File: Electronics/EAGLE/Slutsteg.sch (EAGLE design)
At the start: 149 parts, among them CN1 OSTYK33102030-2, CN2 OSTYK33102030-2, IC1 MC78M12CDTG, IC2 ZLDO1117G33TA, IC3 ESP32-WROVER-IE-4MB, IC4 TM8211, IC5 LM358LVIDR, IC6 TPA3244DDWR, IC7 TPA3251D2DDVR, IC8 LM324D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

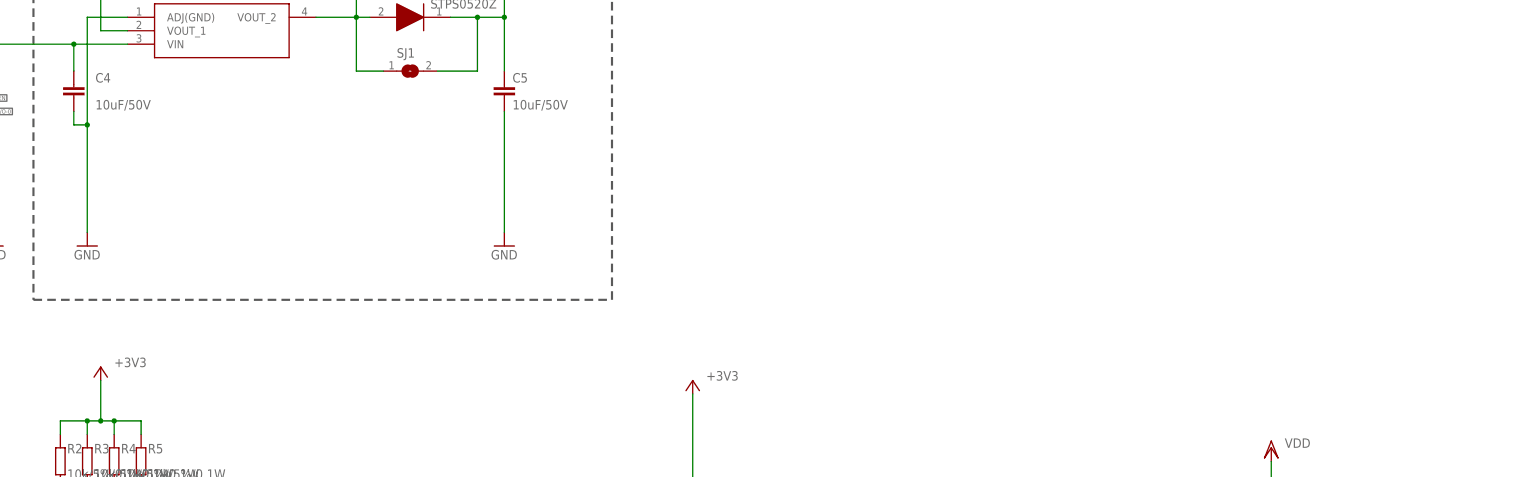
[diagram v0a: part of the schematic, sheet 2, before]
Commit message: Updated components value
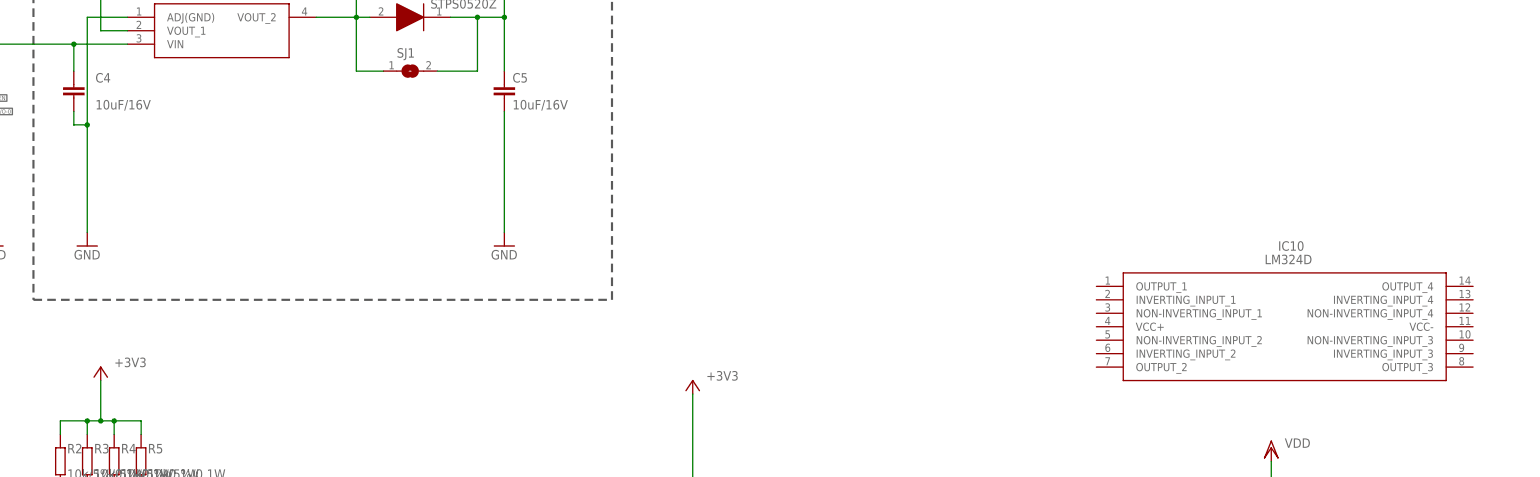
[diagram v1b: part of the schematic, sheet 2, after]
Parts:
- added CN3, CN4: OSTYK33102030-2, OSTYK33108030:OSTYK33102030-2
- added IC10: LM324D, SamacSys_Parts:LM324D
- C4, C5: value 10uF/50V -> 10uF/16V
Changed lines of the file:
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@@
 <part name="P+3" library="supply1" library_urn="urn:adsk.eagle:library:371" deviceset="+5V" device=""/>
 <part name="IC2" library="SamacSys_Parts" deviceset="ZLDO1117G33TA" device="" override_package3d_urn="urn:adsk.eagle:package:27158194/2" override_package_urn="urn:adsk.eagle:footprint:27158195/1"/>
-<part name="C5" library="rcl" library_urn="urn:adsk.eagle:library:334" deviceset="C-EU" device="C0805" package3d_urn="urn:adsk.eagle:package:23617/2" value="10uF/50V"/>
-<part name="C4" library="rcl" library_urn="urn:adsk.eagle:library:334" deviceset="C-EU" device="C0805" package3d_urn="urn:adsk.eagle:package:23617/2" value="10uF/50V"/>
+<part name="C5" library="rcl" library_urn="urn:adsk.eagle:library:334" deviceset="C-EU" device="C0805" package3d_urn="urn:adsk.eagle:package:23617/2" value="10uF/16V"/>
+<part name="C4" library="rcl" library_urn="urn:adsk.eagle:library:334" deviceset="C-EU" device="C0805" package3d_urn="urn:adsk.eagle:package:23617/2" value="10uF/16V"/>
 <part name="GND47" library="supply1" library_urn="urn:adsk.eagle:library:371" deviceset="GND" device=""/>
 <part name="D1" library="SamacSys_Parts" deviceset="STPS0520Z" device="" override_package3d_urn="urn:adsk.eagle:package:27158217/2" override_package_urn="urn:adsk.eagle:footprint:27158218/1"/>
@@
 <part name="R5" library="rcl" library_urn="urn:adsk.eagle:library:334" deviceset="R-EU_" device="R0603" package3d_urn="urn:adsk.eagle:package:23555/3" value="10k/5%/0.1W"/>
 <part name="+3V14" library="supply1" library_urn="urn:adsk.eagle:library:371" deviceset="+3V3" device=""/>
+<part name="IC10" library="SamacSys_Parts" deviceset="LM324D" device=""/>
+<part name="CN3" library="OSTYK33108030" deviceset="OSTYK33102030-2" device="" override_package3d_urn="urn:adsk.eagle:package:27162182/2" override_package_urn="urn:adsk.eagle:footprint:27162183/1"/>
+<part name="CN4" library="OSTYK33108030" deviceset="OSTYK33102030-2" device="" override_package3d_urn="urn:adsk.eagle:package:27162207/2" override_package_urn="urn:adsk.eagle:footprint:27162209/1"/>
 </parts>
 <sheets>
@@
 <instance part="CN2" gate="G$1" x="342.9" y="182.88" smashed="yes">
 <attribute name="NAME" x="342.9" y="200.66" size="1.778" layer="95"/>
+</instance>
+<instance part="CN3" gate="G$1" x="342.9" y="149.86" smashed="yes">
+<attribute name="NAME" x="342.9" y="167.64" size="1.778" layer="95"/>
+</instance>
+<instance part="CN4" gate="G$1" x="342.9" y="121.92" smashed="yes">
+<attribute name="NAME" x="342.9" y="139.7" size="1.778" layer="95"/>
 </instance>
 </instances>
@@
 <attribute name="VALUE" x="68.58" y="127" size="1.778" layer="96"/>
 </instance>
+<instance part="IC10" gate="G$1" x="254" y="142.24" smashed="yes">
+<attribute name="NAME" x="288.29" y="149.86" size="1.778" layer="95" align="center-left"/>
+<attribute name="VALUE" x="285.75" y="147.32" size="1.778" layer="96" align="center-left"/>
+</instance>
 </instances>

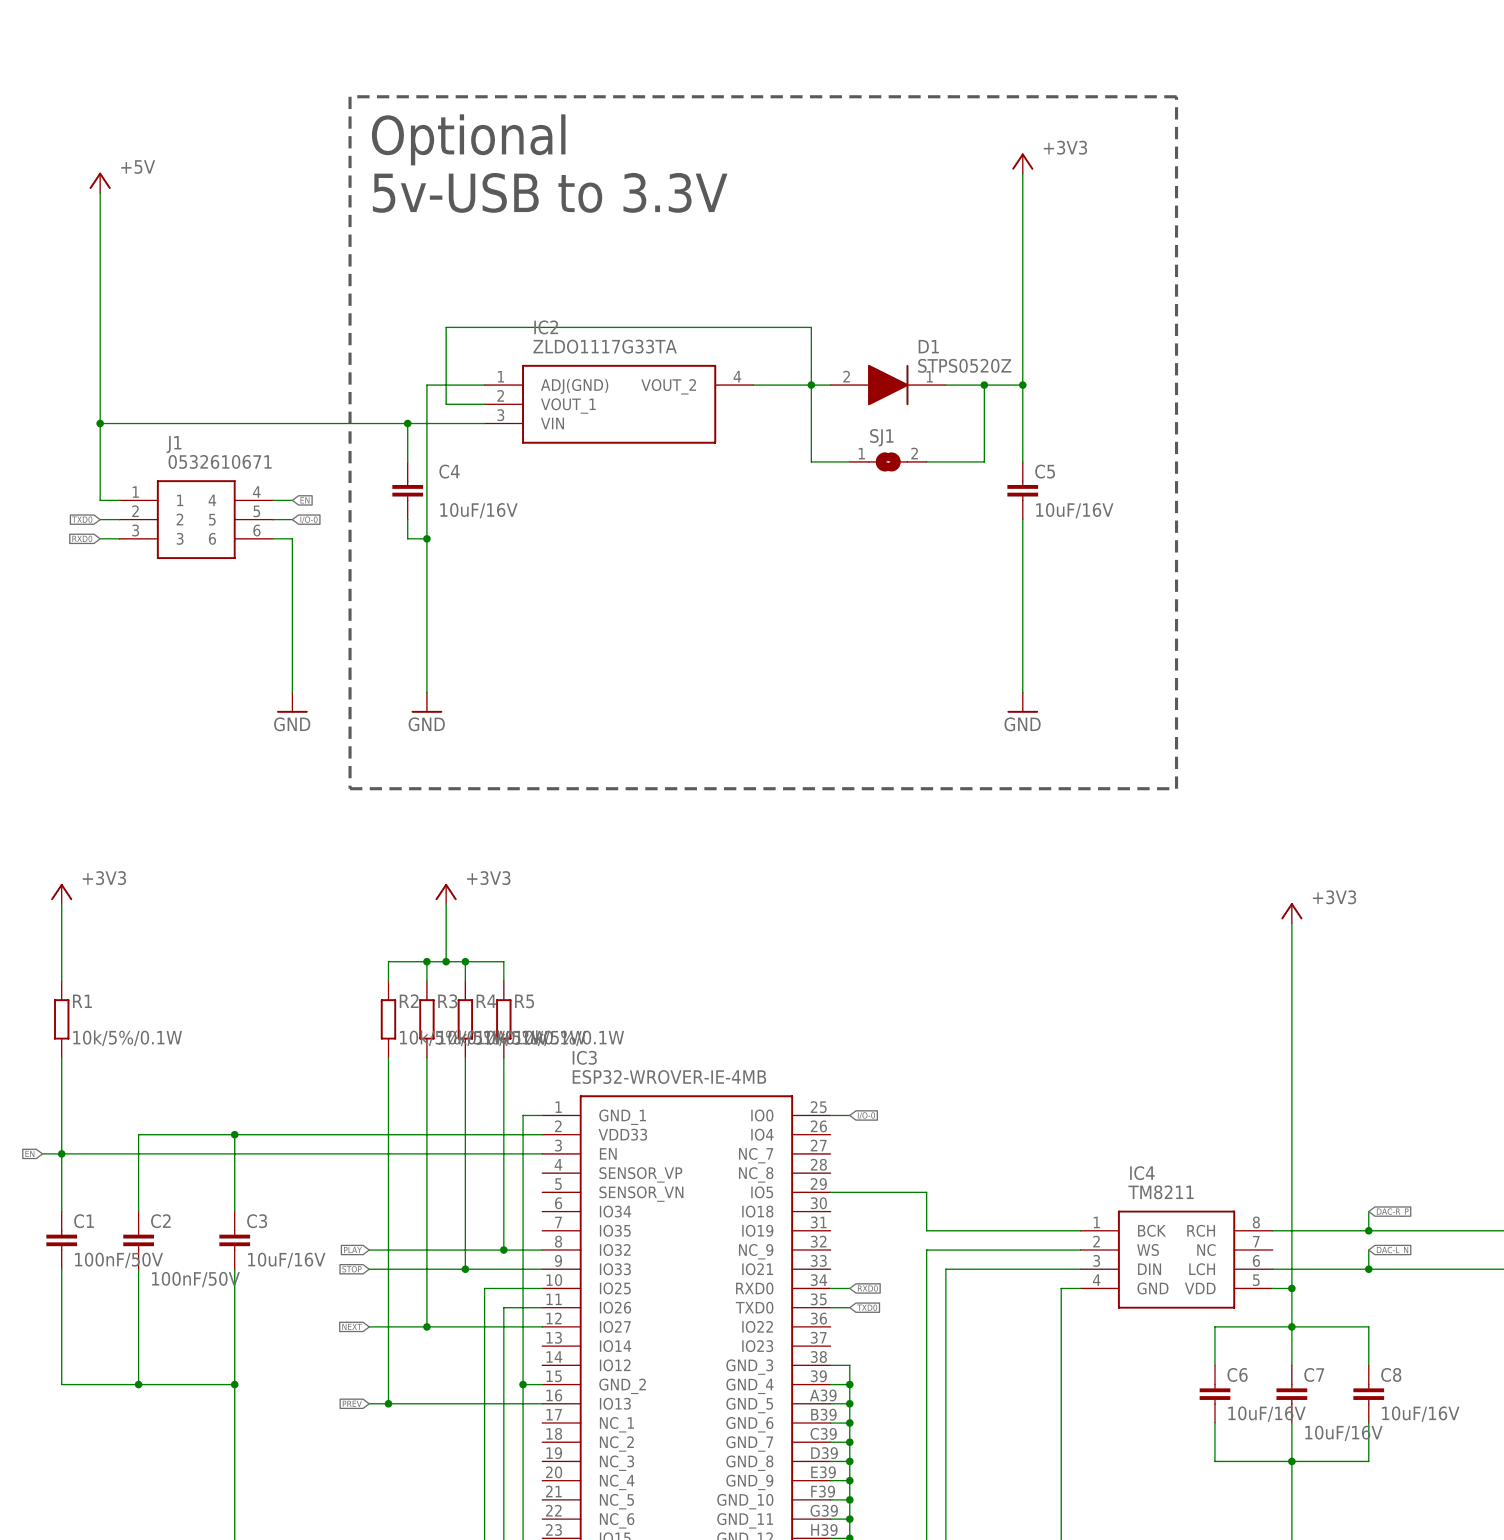
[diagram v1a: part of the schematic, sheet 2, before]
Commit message: Changed some component footprints and simplified the V-Reg configuration
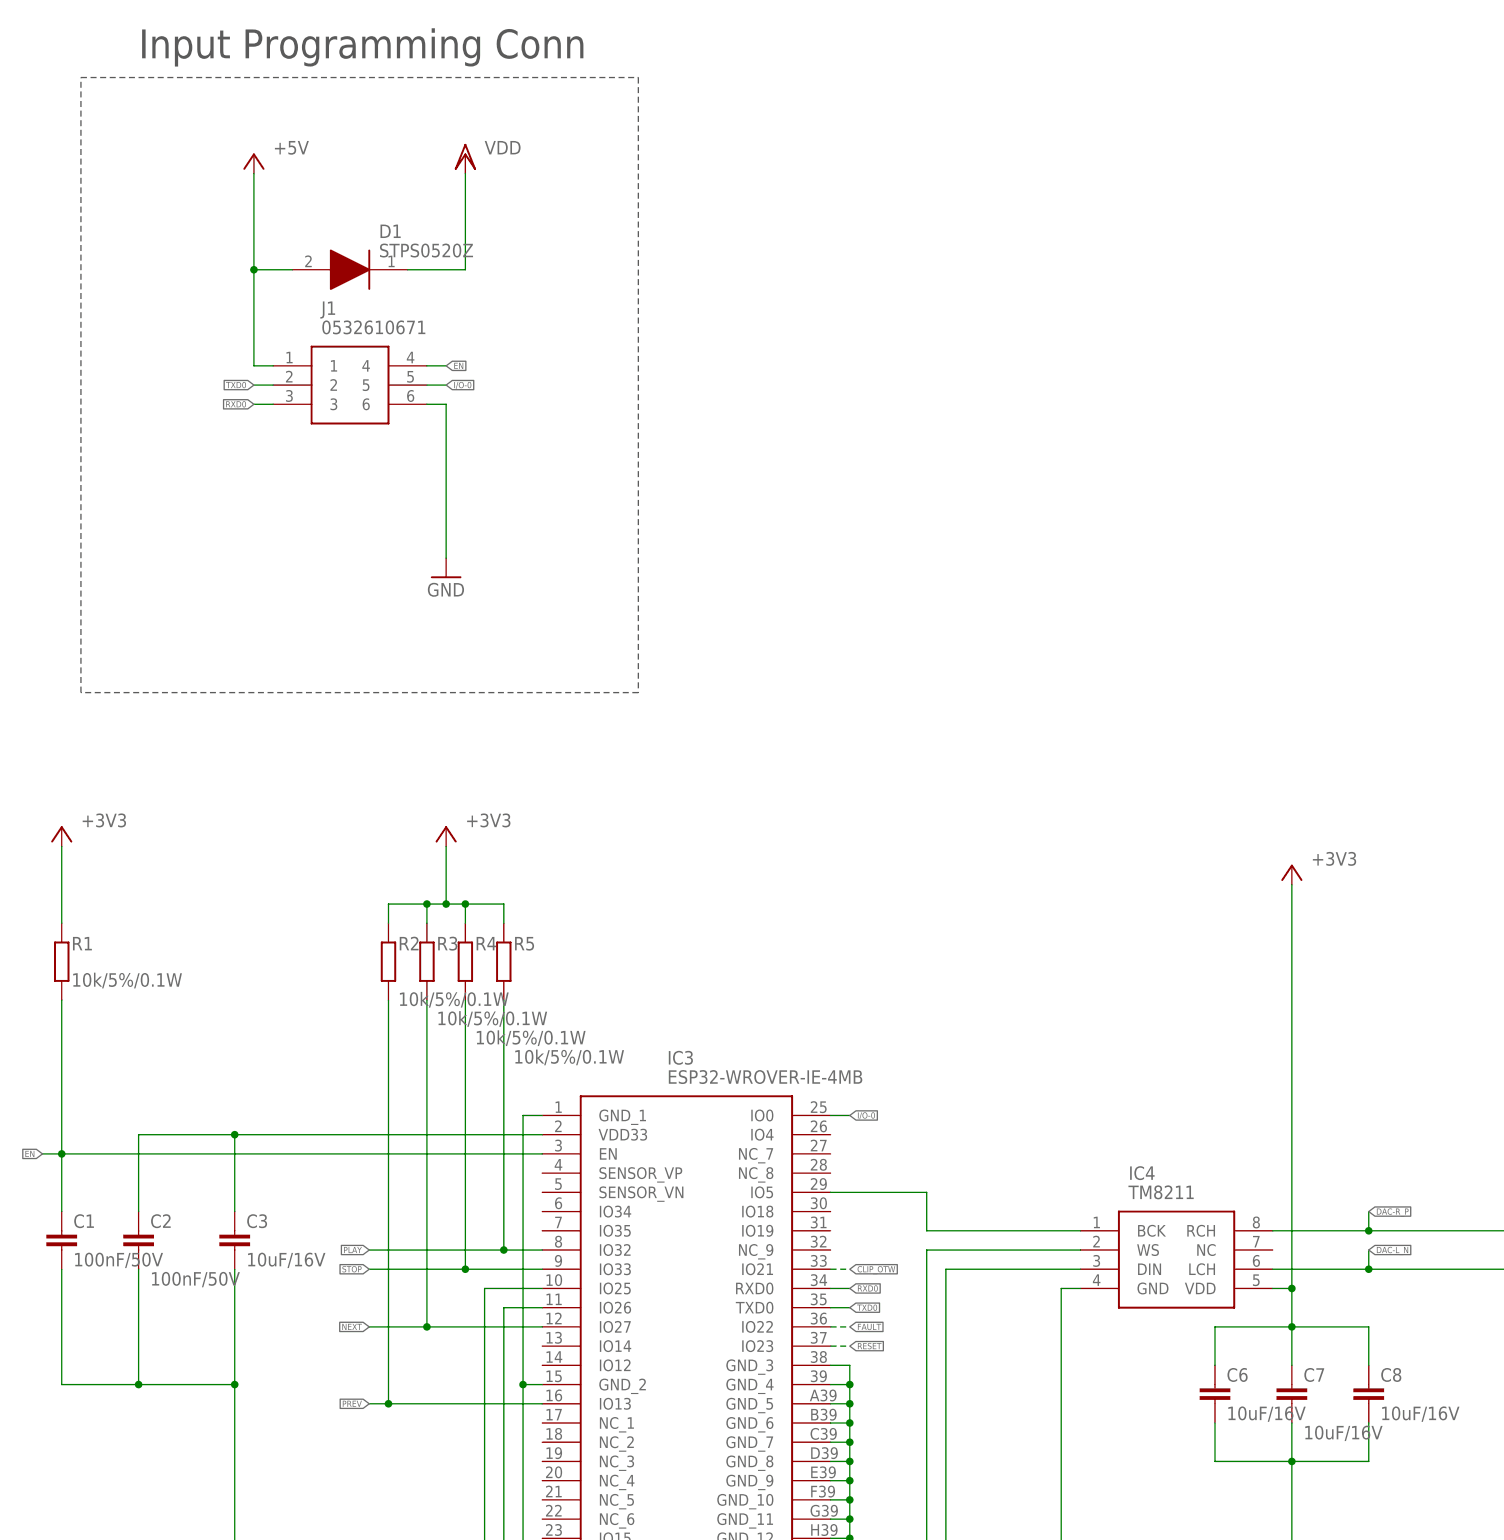
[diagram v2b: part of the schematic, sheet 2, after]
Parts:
- removed C25: 10uF/16V, rcl:C-EUC1206
- removed IC2: ZLDO1117G33TA, SamacSys_Parts:ZLDO1117G33TA
- removed SJ1: (no value), jumper:SJ
- added C82: 10uF/16V, rcl:C-EUC0805
- added IC11: L78M12ABDT-TR, SamacSys_Parts:L78M12ABDT-TR
- C21, C22, C24: device rcl:C-EUC1206 -> rcl:C-EUC0805
- C6: device rcl:C-EUC0603 -> rcl:C-EUC0805
- IC1: value MC78M12CDTG -> SPX1117M3-L-3-3_TR; device linear:MC78M12CDTG -> SamacSys_Parts:SPX1117M3-L-3-3_TR
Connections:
- removed net N$43: D1.A, IC2.VOUT_1, IC2.VOUT_2, SJ1.1
- net +3V3: now also IC1.VOUT_1, IC1.VOUT_2; no longer D1.K, SJ1.2
- net +5V: now also D1.A; no longer C4.1, IC2.VIN
- net CLIP_OTW: now also IC3.IO21
- net FAULT: now also IC3.IO22
- net GND: now also IC1.ADJ/GND, IC11.GND_(THERMALPAD); no longer IC1.GND, IC2.ADJ(GND)
- net INPUT_A: now also C22.1; no longer C22.2
- net INPUT_B: now also C24.1; no longer C25.2
- net INPUT_C: now also C21.1; no longer C21.2
- net INPUT_D: now also C82.1; no longer C24.2
- net N$61: now also C82.2; no longer C24.1
- net N$62: now also C21.2; no longer C21.1
- net N$63: now also C24.2; no longer C25.1
- net N$64: now also C22.2; no longer C22.1
- net PVDD: now also IC11.INPUT
- net RESET: now also IC3.IO23
- net VDD: now also C4.1, D1.K, IC1.VIN, IC11.OUTPUT
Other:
- note added: "Input Programming Conn"
- note removed: "Optional 5v-USB to 3.3V"
- moved on the sheet: C21, C22, C24, D1, J1, R1, R2, R3, R4, R5
